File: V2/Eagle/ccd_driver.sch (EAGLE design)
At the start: 48 parts, among them IC1 74HC04D, IC3 FT232RL, J1 USB-MINIB-5PIN, Q1 BC214, U2 MK02FN128VLF10

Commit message: Changed fM,SH,ICG pins to match with timers, added TODO list, cleaned up schematics and add them to different sheets
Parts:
- removed C6, C7, C8: 0.1 µF, resistor:C-EUC1206
- removed C9: 10uF, resistor:C-EUC1206
- removed IC3: FT232RL, ftdichip:FT232RL
- removed J1: USB-MINIB-5PIN, SparkFun-Connectors:USB-MINIB-5PIN
- removed Q1: BC214, transistor-pnp:BC214
- removed R12, R13, R14: 0, resistor:R-US_R0805
- removed R15: 5.9k, resistor:R-US_R0805
- removed R17, R18: 11k, resistor:R-US_R0805
- removed R19: 10.5k, resistor:R-US_R0805
- removed R5, R6: 22, resistor:R-US_R0805
- removed R7, R8: 1k, resistor:R-US_R0805
- removed RX_LED, TX_LED: (no value), led:LEDCHIPLED_0805
- removed TP1, TP2, TP3: TPPAD1-17Y, testpad:TPPAD1-17Y
- removed U$3: LTC6252, ccd:LTC6252
- removed U$4: LD1117V33, ccd:LD1117V33
- added C15: 10uF, resistor:C-EUC1206
- added C4: 0.1µF, resistor:C-EUC1206
- added J2: USB-MINIB-5PIN, SparkFun-Connectors:USB-MINIB-5PIN
- added Q2: BC214, transistor-pnp:BC214
- added R20: 69.8k, resistor:R-US_R0805
- added R21: 5.9k, resistor:R-US_R0805
- added R22, R23: 11k, resistor:R-US_R0805
- added R24: 10.5k, resistor:R-US_R0805
- added R25, R26: 150, resistor:R-US_R0805
- added R27: 2200, resistor:R-US_R0805
- added R28, R29, R30: 0, resistor:R-US_R0805
- added RX_LED1, TX_LED1: (no value), led:LEDCHIPLED_0805
- added TP4, TP5, TP6: TPPAD1-17Y, testpad:TPPAD1-17Y
- added U$2: TCD1304, ccd:TCD1304
- added U$5: LTC6252, ccd:LTC6252
- C2: value 10uF -> 0.1 µF
- C3: value 0.1µF -> 0.1 µF
- IC1: value 74HC04D -> FT232RL; device 74xx-eu:74HC04D -> ftdichip:FT232RL
- R1: value 69.8k -> 22
- R10: value 150 -> 1k
- R11: value 2200 -> 1k
- R9: value 150 -> 22
- U$1: value TCD1304 -> LD1117V33; device ccd:TCD1304 -> ccd:LD1117V33
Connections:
- removed net BU: Q1.E, R11.2, R14.1
- removed net N$14: J1.D-, R5.2
- removed net N$16: J1.D+, R6.2
- removed net N$17: C7.1, C8.2, IC3.3V3OUT, IC3.VCCIO
- removed net N$18: IC3.CBUS0, R7.1
- removed net N$19: IC3.USBDM, R5.1
- removed net N$20: IC3.USBDP, R6.1
- removed net N$21: IC3.CBUS1, R8.1
- removed net N$22: R8.2, RX_LED.C
- removed net N$23: R7.2, TX_LED.C
- new net BU1: Q2.E, R27.2, R30.1
- new net N$28: R23.2, R24.1, U$5.+
- new net N$29: R24.2, R28.1, U$2.21
- new net N$30: Q2.B, R25.1
- new net N$31: Q2.C, R26.1
- new net N$32: R25.2, R28.2
- new net N$6: R20.1, R21.2, R22.2, U$5.-
- net 3.3V: now also C15.1, C4.1, TP5.TP, U$1.VOUT, U$2.1, U$2.2; no longer C3.1, C9.1, TP1.TP, U$1.1, U$1.2, U$4.VOUT
- net 5V: now also C3.1, IC1.!RESET, IC1.VCC, J2.VBUS, R20.2, R27.1, RX_LED1.A, TP4.TP, TX_LED1.A, U$1.VIN, U$5.V+; no longer C1.1, C6.1, C8.1, IC1P.VCC, IC3.!RESET, IC3.VCC, J1.VBUS, R1.2, R11.1, RX_LED.A, TP2.TP, TX_LED.A, U$3.V+, U$4.VIN
- net AGND: now also C4.2, R21.1, R23.1, R26.2, R29.1, U$2.10, U$2.11, U$2.12, U$2.13, U$2.14, U$2.15, U$2.16, U$2.17, U$2.18, U$2.19, U$2.20, U$2.22, U$2.6, U$2.7, U$2.8, U$2.9, U$5.V-; no longer C3.2, R10.2, R13.1, R15.1, R18.1, U$1.10, U$1.11, U$1.12, U$1.13, U$1.14, U$1.15, U$1.16, U$1.17, U$1.18, U$1.19, U$1.20, U$1.22, U$1.6, U$1.7, U$1.8, U$1.9, U$3.V-
- net FM: now also U$2.4, U2.PTC1/LLWU_P6; no longer IC1B.I, U2.PTB3
- net GND: now also C15.2, C3.2, IC1.GND, IC1.GND@1, IC1.GND@2, IC1.GND@A, IC1.TEST, J2.GND, R29.2, TP6.TP, U$1.GND; no longer C2.2, C6.2, C7.2, C9.2, IC1P.GND, IC3.GND, IC3.GND@1, IC3.GND@2, IC3.GND@A, IC3.TEST, J1.GND, R13.2, TP3.TP, U$4.GND
- net ICG: now also U$2.3, U2.PTB1; no longer IC1A.I, U2.PTB16
- net N$1: now also IC1.USBDM, R1.1; no longer R18.2, R19.1, U$3.+
- net N$10: now also R11.2, RX_LED1.C; no longer R12.1, R19.2, U$1.21
- net N$11: now also U2.PTB3; no longer U2.PTB1
- net N$15: now also U2.PTB2; no longer U2.PTB0/LLWU_P5
- net N$2: now also IC1.USBDP, R9.1; no longer IC1A.O, U$1.3
- net N$24: now also R10.2, TX_LED1.C; no longer R12.2, R9.2
- net N$3: now also J2.D-, R1.2; no longer IC1B.O, U$1.4
- net N$4: now also J2.D+, R9.2; no longer IC1C.O, U$1.5
- net N$5: now also C1.1, C2.2, IC1.3V3OUT, IC1.VCCIO; no longer Q1.B, R9.1
- net N$8: now also IC1.CBUS0, R10.1; no longer R1.1, R15.2, R17.2, U$3.-
- net N$9: now also IC1.CBUS1, R11.1; no longer Q1.C, R10.1
- net OS: now also R22.1, R30.2, U$5.OUT; no longer R14.2, R17.1, U$3.OUT, U2.PTE19
- net PCRX: now also IC1.TXD; no longer IC3.TXD
- net PCTX: now also IC1.RXD; no longer IC3.RXD
- net SH: now also U$2.5, U2.PTB0/LLWU_P5; no longer IC1C.I, U2.PTB2
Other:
- note added: "TODO: A bit of EEPROM"
- note added: "TODO: Add motor control for fan"
- note added: "TODO: Add peltier element, thermistors"
- note added: "TODO: Add proper power supply"
- note added: "TODO: Add some sort of LCD interface + encoder"
- note added: "TODO: Change USB, add input protection"
- note added: "TODO: Fix amplifier, add unity gain amp"
- note added: "TODO: Halogen lamp drivers"
- note added: "TODO: LED Drivers"
- note added: "TODO: OS to external ADC?"
- note added: "TODO: Precision Voltage Ref"
- note removed: "Decoupling"

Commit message: added micro sd card
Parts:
- added C5: 100nF, resistor:C-EUC1206
- added C6: 100uF, resistor:C-EUC1206
- added U$3: MICROSD-PUSH-OUT, microsd:MICROSD-PUSH-OUT
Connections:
- new net SD_CLK: U$3.CLK
- new net SD_CS: U$3.CD_DAT3_CS
- new net SD_DI: U$3.CMD_DIN
- new net SD_DO: U$3.DAT0_DO
- net 3.3V: now also C5.1, C6.1, U$3.VDD
- net GND: now also C5.2, C6.2, U$3.VSS
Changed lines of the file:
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@@
 <part name="GND18" library="supply1" library_urn="urn:adsk.eagle:library:371" deviceset="GND" device=""/>
 <part name="FRAME4" library="frames" library_urn="urn:adsk.eagle:library:229" deviceset="FRAME_A_L" device=""/>
+<part name="FRAME5" library="frames" library_urn="urn:adsk.eagle:library:229" deviceset="FRAME_A_L" device=""/>
+<part name="U$3" library="microsd" deviceset="MICROSD-PUSH-OUT" device=""/>
+<part name="GND5" library="supply1" library_urn="urn:adsk.eagle:library:371" deviceset="GND" device=""/>
+<part name="SUPPLY12" library="SparkFun-Aesthetics" library_urn="urn:adsk.eagle:library:507" deviceset="3.3V" device=""/>
+<part name="C5" library="resistor" library_urn="urn:adsk.eagle:library:348" deviceset="C-EU" device="C1206" package3d_urn="urn:adsk.eagle:package:23618/2" value="100nF"/>
+<part name="C6" library="resistor" library_urn="urn:adsk.eagle:library:348" deviceset="C-EU" device="C1206" package3d_urn="urn:adsk.eagle:package:23618/2" value="100uF"/>
+<part name="GND1" library="supply1" library_urn="urn:adsk.eagle:library:371" deviceset="GND" device=""/>
+<part name="SUPPLY1" library="SparkFun-Aesthetics" library_urn="urn:adsk.eagle:library:507" deviceset="3.3V" device=""/>
 </parts>
 <sheets>
@@
 </segment>
 </bus>
+<bus name="SPI:SD_CLK,SD_CS,SD_DI,SD_DO,SPI">
+<segment>
+<wire x1="10.16" y1="152.4" x2="10.16" y2="139.7" width="0.762" layer="92"/>
+<wire x1="10.16" y1="139.7" x2="7.62" y2="137.16" width="0.762" layer="92"/>
+<label x="8.89" y="139.7" size="1.778" layer="95" rot="R90"/>
+</segment>
+</bus>
 </busses>
 <nets>
@@
 <pinref part="R16" gate="G$1" pin="1"/>
 <junction x="233.68" y="137.16"/>
+</segment>
+</net>
+<net name="SD_CS" class="0">
+<segment>
+<wire x1="25.4" y1="152.4" x2="12.7" y2="152.4" width="0.1524" layer="91"/>
+<label x="12.7" y="152.4" size="1.778" layer="95"/>
+<wire x1="10.16" y1="149.86" x2="12.7" y2="152.4" width="0.1524" layer="91"/>
+</segment>
+</net>
+<net name="SD_DI" class="0">
+<segment>
+<wire x1="10.16" y1="147.32" x2="12.7" y2="149.86" width="0.1524" layer="91"/>
+<wire x1="25.4" y1="149.86" x2="12.7" y2="149.86" width="0.1524" layer="91"/>
+<label x="12.7" y="149.86" size="1.778" layer="95"/>
+</segment>
+</net>
+<net name="SD_CLK" class="0">
+<segment>
+<wire x1="25.4" y1="147.32" x2="12.7" y2="147.32" width="0.1524" layer="91"/>
+<label x="12.7" y="147.32" size="1.778" layer="95"/>
+<wire x1="10.16" y1="144.78" x2="12.7" y2="147.32" width="0.1524" layer="91"/>
+</segment>
+</net>
+<net name="SD_DO" class="0">
+<segment>
+<wire x1="25.4" y1="144.78" x2="12.7" y2="144.78" width="0.1524" layer="91"/>
+<label x="12.7" y="144.78" size="1.778" layer="95"/>
+<wire x1="10.16" y1="142.24" x2="12.7" y2="144.78" width="0.1524" layer="91"/>
 </segment>
 </net>
@@
 </segment>
 </net>
+</nets>
+</sheet>
+<sheet>
+<plain>
+</plain>
+<instances>
+<instance part="FRAME5" gate="G$1" x="0" y="0"/>
+<instance part="FRAME5" gate="G$2" x="172.72" y="0"/>
+<instance part="U$3" gate="G$1" x="195.58" y="129.54"/>
+<instance part="GND5" gate="1" x="124.46" y="114.3"/>
+<instance part="SUPPLY12" gate="G$1" x="124.46" y="127"/>
+<instance part="C5" gate="G$1" x="86.36" y="124.46"/>
+<instance part="C6" gate="G$1" x="76.2" y="124.46"/>
+<instance part="GND1" gate="1" x="76.2" y="116.84"/>
+<instance part="SUPPLY1" gate="G$1" x="76.2" y="127"/>
+</instances>
+<busses>
+<bus name="SPI:SD_CLK,SD_CS,SD_DI,SD_DO,SPI">
+<segment>
+<wire x1="101.6" y1="139.7" x2="101.6" y2="106.68" width="0.762" layer="92"/>
+<wire x1="101.6" y1="106.68" x2="99.06" y2="104.14" width="0.762" layer="92"/>
+<label x="100.33" y="106.68" size="1.778" layer="95" rot="R90"/>
+</segment>
+</bus>
+</busses>
+<nets>
+<net name="GND" class="0">
+<segment>
+<pinref part="U$3" gate="G$1" pin="VSS"/>
+<wire x1="127" y1="116.84" x2="124.46" y2="116.84" width="0.1524" layer="91"/>
+<pinref part="GND5" gate="1" pin="GND"/>
+</segment>
+<segment>
+<pinref part="C6" gate="G$1" pin="2"/>
+<pinref part="C5" gate="G$1" pin="2"/>
+<wire x1="76.2" y1="119.38" x2="86.36" y2="119.38" width="0.1524" layer="91"/>
+<pinref part="GND1" gate="1" pin="GND"/>
+<junction x="76.2" y="119.38"/>
+</segment>
+</net>
+<net name="3.3V" class="0">
+<segment>
+<pinref part="U$3" gate="G$1" pin="VDD"/>
+<wire x1="127" y1="127" x2="124.46" y2="127" width="0.1524" layer="91"/>
+<pinref part="SUPPLY12" gate="G$1" pin="3.3V"/>
+</segment>
+<segment>
+<pinref part="C6" gate="G$1" pin="1"/>
+<pinref part="C5" gate="G$1" pin="1"/>
+<wire x1="76.2" y1="127" x2="86.36" y2="127" width="0.1524" layer="91"/>
+<pinref part="SUPPLY1" gate="G$1" pin="3.3V"/>
+<junction x="76.2" y="127"/>
+</segment>
+</net>
+<net name="SD_CS" class="0">
+<segment>
+<pinref part="U$3" gate="G$1" pin="CD_DAT3_CS"/>
+<wire x1="127" y1="137.16" x2="104.14" y2="137.16" width="0.1524" layer="91"/>
+<label x="104.14" y="137.16" size="1.778" layer="95"/>
+<wire x1="101.6" y1="134.62" x2="104.14" y2="137.16" width="0.1524" layer="91"/>
+</segment>
+</net>
+<net name="SD_DI" class="0">
+<segment>
+<wire x1="101.6" y1="129.54" x2="104.14" y2="132.08" width="0.1524" layer="91"/>
+<pinref part="U$3" gate="G$1" pin="CMD_DIN"/>
+<wire x1="127" y1="132.08" x2="104.14" y2="132.08" width="0.1524" layer="91"/>
+<label x="104.14" y="132.08" size="1.778" layer="95"/>
+</segment>
+</net>
+<net name="SD_CLK" class="0">
+<segment>
+<pinref part="U$3" gate="G$1" pin="CLK"/>
+<wire x1="127" y1="121.92" x2="104.14" y2="121.92" width="0.1524" layer="91"/>
+<label x="104.14" y="121.92" size="1.778" layer="95"/>
+<wire x1="101.6" y1="119.38" x2="104.14" y2="121.92" width="0.1524" layer="91"/>
+</segment>
+</net>
+<net name="SD_DO" class="0">
+<segment>
+<pinref part="U$3" gate="G$1" pin="DAT0_DO"/>
+<wire x1="127" y1="111.76" x2="104.14" y2="111.76" width="0.1524" layer="91"/>
+<label x="104.14" y="111.76" size="1.778" layer="95"/>
+<wire x1="101.6" y1="109.22" x2="104.14" y2="111.76" width="0.1524" layer="91"/>
+</segment>
+</net>

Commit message: added peltier driver: MOSFET w/ LPF, 12V 5A
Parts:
- added 1410460C: 100uH, DMN1019UVT:1410460C
- added C9: 47uF, SparkFun-Capacitors:10UF-1210-50V-20%
- added J1: (no value), SparkFun-Connectors:CONN_022.54MM_SCREWTERM
- added U$4: DMN1019UVT, DMN1019UVT:DMN1019UVT
- added U$6: DB2431200L, DMN1019UVT:DB2431200L
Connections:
- new net +12V: C9.1, J1.1, U$6.-
- new net N$16: 1410460C.2, C9.2, J1.2
- new net N$17: 1410460C.1, U$4.D, U$6.+
- new net PELT0_ON: U$4.G
- net GND: now also U$4.S
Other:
- note added: "+"
- note added: "-"
- note added: "12V 5A Maximum"
- note added: "LPF: 2321.5 Hz Cutoff"
- note added: "Peltier"
- note added: "TODO: A bit of EEPROM [X] Added SPI SD card"
- note added: "TODO: Add peltier element, thermistors [X]"
- note removed: "TODO: A bit of EEPROM"
- note removed: "TODO: Add peltier element, thermistors"

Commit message: added LTSpice sch for pelt driver
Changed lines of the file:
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@@
 <part name="1410460C" library="DMN1019UVT" deviceset="1410460C" device="" value="100uH"/>
 <part name="U$6" library="DMN1019UVT" deviceset="DB2431200L" device=""/>
+<part name="FRAME7" library="frames" library_urn="urn:adsk.eagle:library:229" deviceset="FRAME_A_L" device=""/>
 </parts>
 <sheets>
@@
 </nets>
 </sheet>
+<sheet>
+<plain>
+</plain>
+<instances>
+<instance part="FRAME7" gate="G$1" x="0" y="0"/>
+<instance part="FRAME7" gate="G$2" x="172.72" y="0"/>
+</instances>
+<busses>
+</busses>
+<nets>
+</nets>
+</sheet>

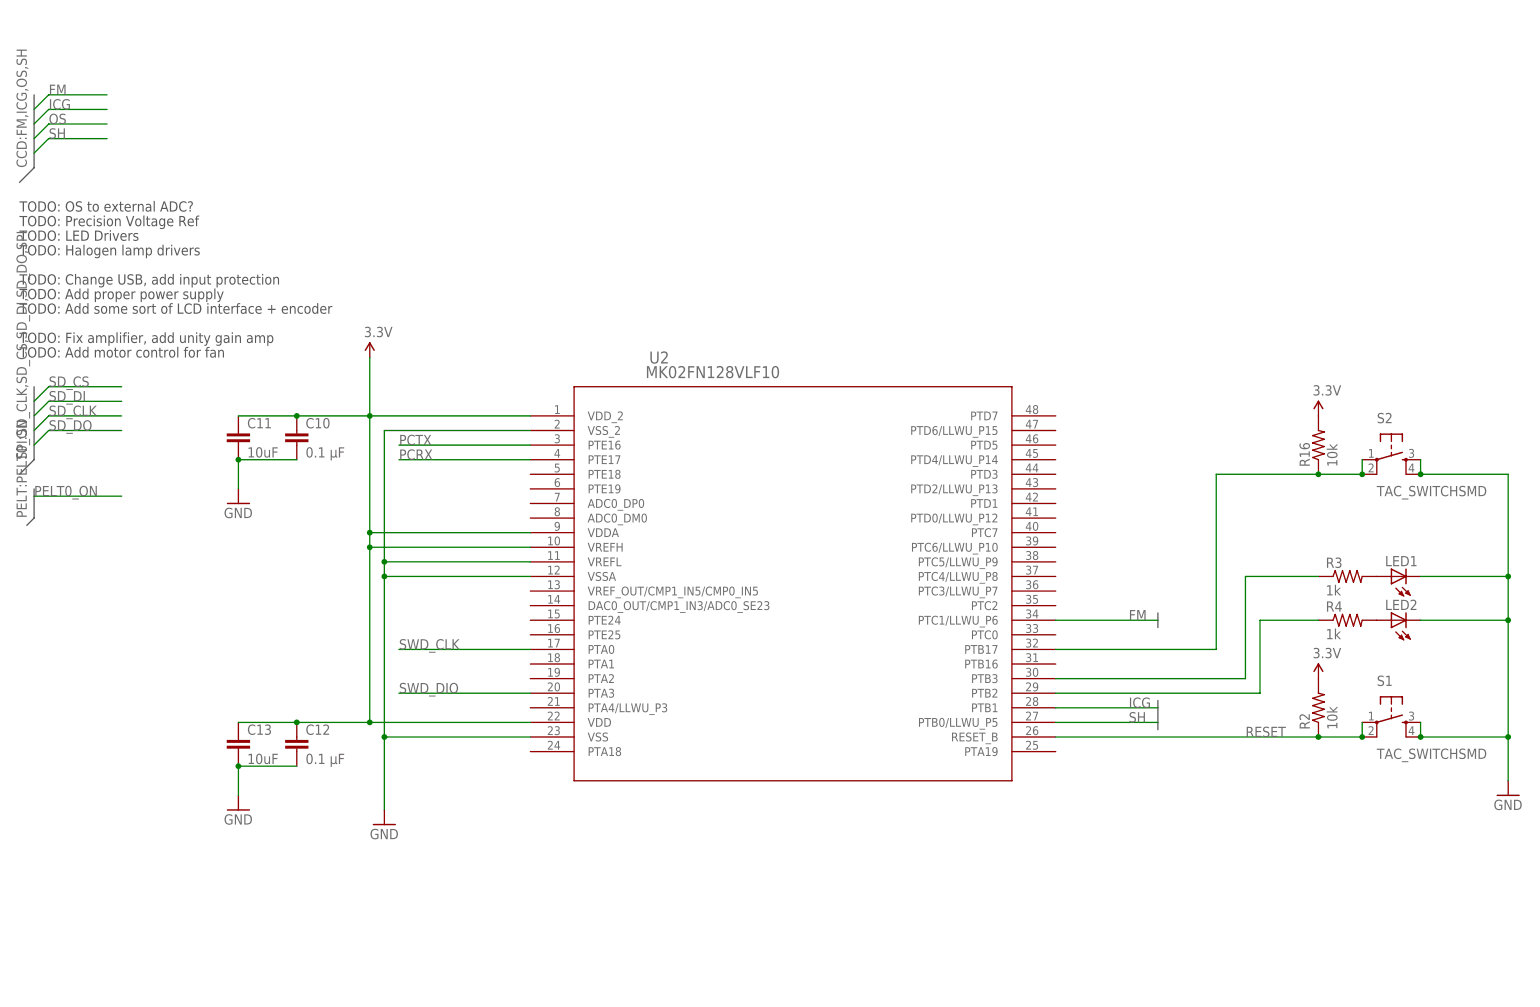
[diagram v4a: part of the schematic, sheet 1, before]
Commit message: added 36V tolerant buck reg -> 3.3V 3A
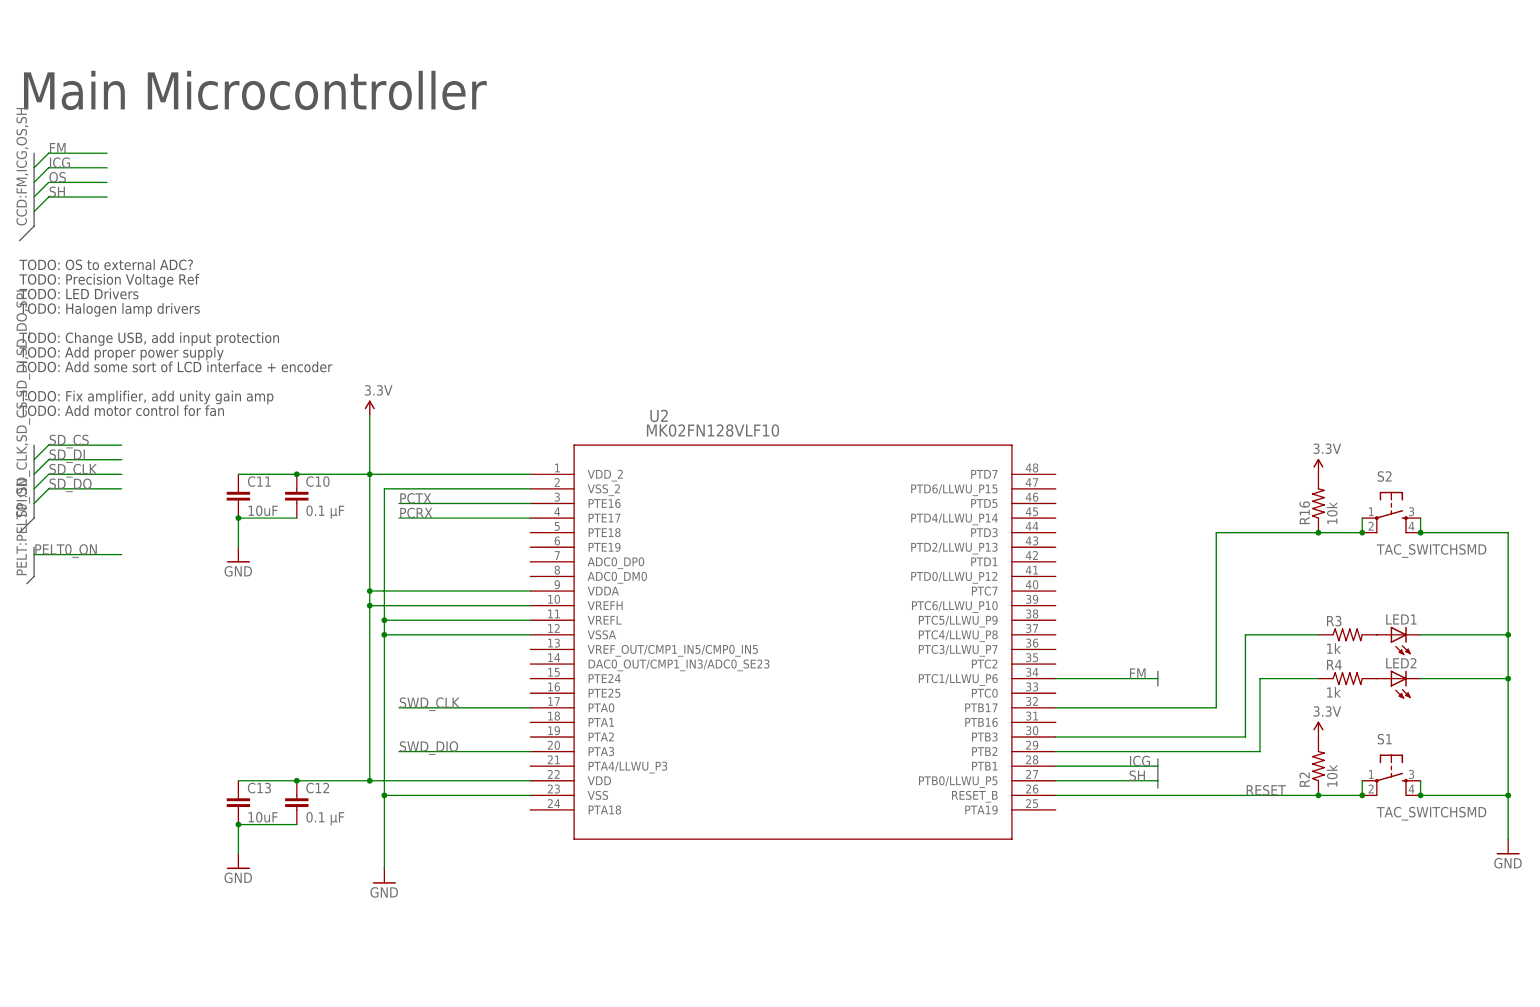
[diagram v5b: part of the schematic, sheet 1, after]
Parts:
- added 486R8SC: 6.8 uF, LMR23630:486R8SC
- added C42: 10uF, SparkFun-Capacitors:10UF-1210-50V-20%
- added C43: 2.2uF, SparkFun-Capacitors:10PF-50V-5%(0603)
- added C44: 75 pF, SparkFun-Capacitors:10PF-50V-5%(0603)
- added C45: 470 nF, SparkFun-Capacitors:10PF-50V-5%(0603)
- added J3: POWER_JACK, SparkFun-Connectors:POWER_JACK
- added R18: 22.1k, audio amplifier example:R-US_R0603
- added R19: 51k, audio amplifier example:R-US_R0603
- added U$7: LMR23630, LMR23630:LMR23630
- added U$8: R1966ABLKBLKFR, LMR23630:R1966ABLKBLKFR
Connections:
- new net N$14: C43.1, U$7.VCC
- new net N$18: 486R8SC.1, C45.2, U$7.SW
- new net N$21: C42.1, U$7.EN/SYNC, U$7.VIN, U$8.2
- new net N$25: C44.2, R18.2, R19.1, U$7.FB
- new net N$33: C45.1, U$7.BOOT
- new net N$34: 486R8SC.2, C44.1, R19.2
- new net N$35: J3.PWR, U$8.1
- net GND: now also C42.2, C43.2, J3.GND, J3.GNDBREAK, R18.1, U$7.AGND, U$7.PGND
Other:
- note added: "36V Tolerant Input, 3.3V Out"
- note added: "CCD & Amp"
- note added: "Main Microcontroller"
- note added: "Peltier Cooler Driver"
- note added: "Power"
- note added: "SD Card"
- note added: "USB"
- note added: "X7R || X5R >=16V"
- moved on the sheet: C10, C11, C12, C13, LED1, LED2, R16, R2, R3, R4, S1, S2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
